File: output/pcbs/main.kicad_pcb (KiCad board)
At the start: 2 copper layers, 121 x 101.5 mm, 62 parts

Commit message: fix PCB + add quirk to readme
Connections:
- _20 pad : GND -> P2
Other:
- net class Default removed

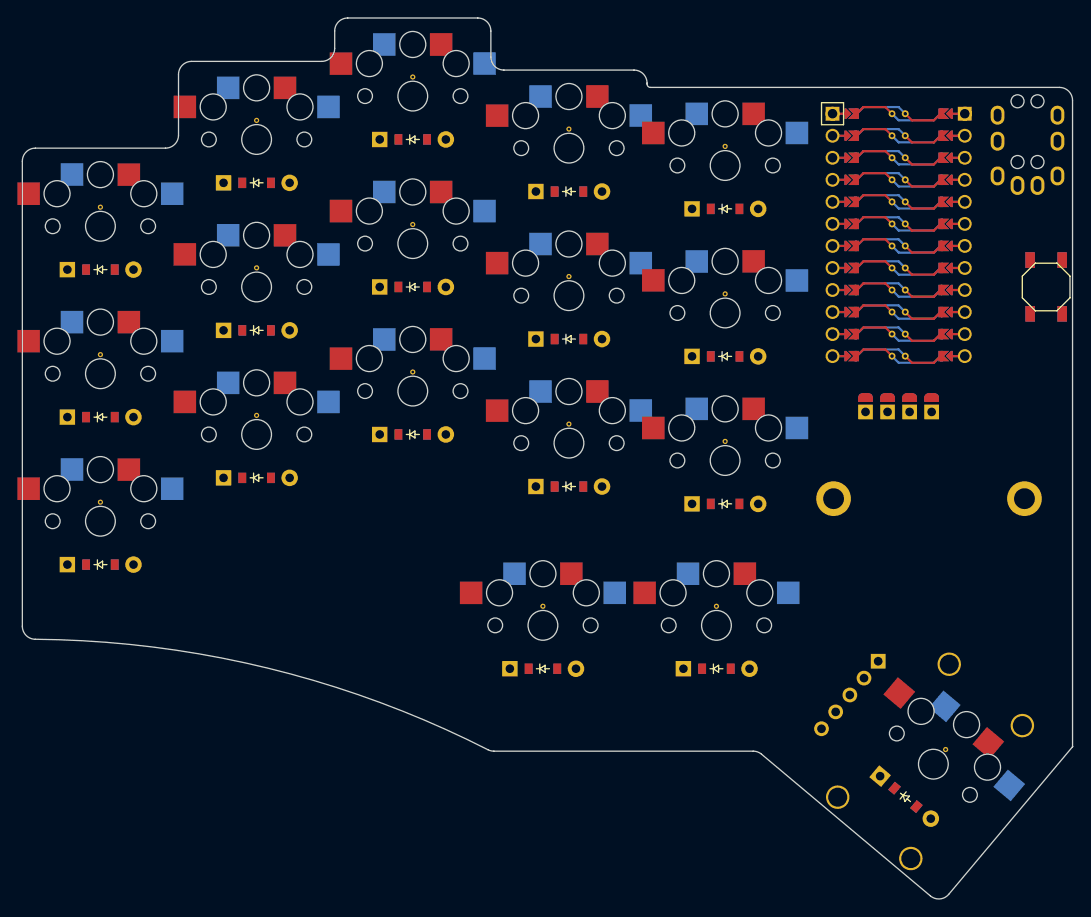
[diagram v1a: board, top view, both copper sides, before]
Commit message: temporary fix to turn trackball around
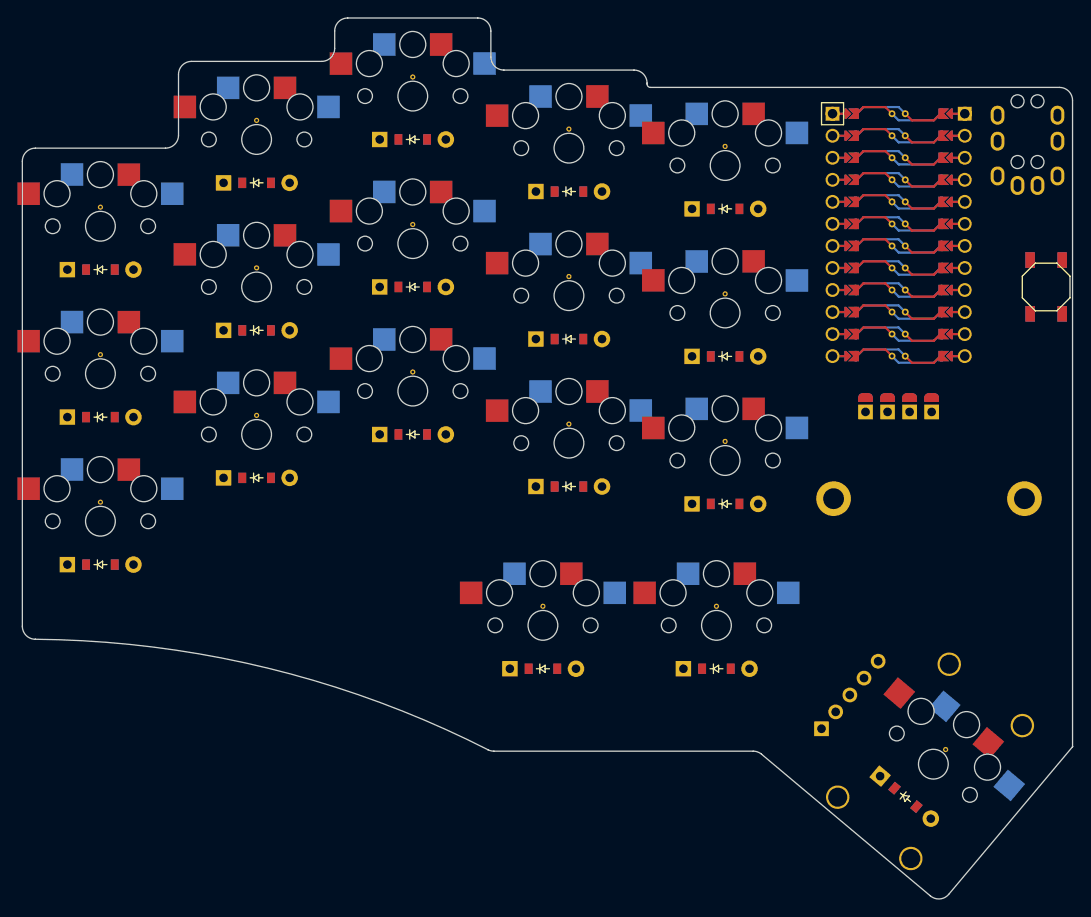
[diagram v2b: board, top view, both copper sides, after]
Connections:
- _20 pad : P2 -> VCC
- _21 pad 3: VCC, -> VCC
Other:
- net class Default added: clearance 0.2, trace_width 0.25, via_dia 0.8, via_drill 0.4

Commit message: whoops the vias were too close
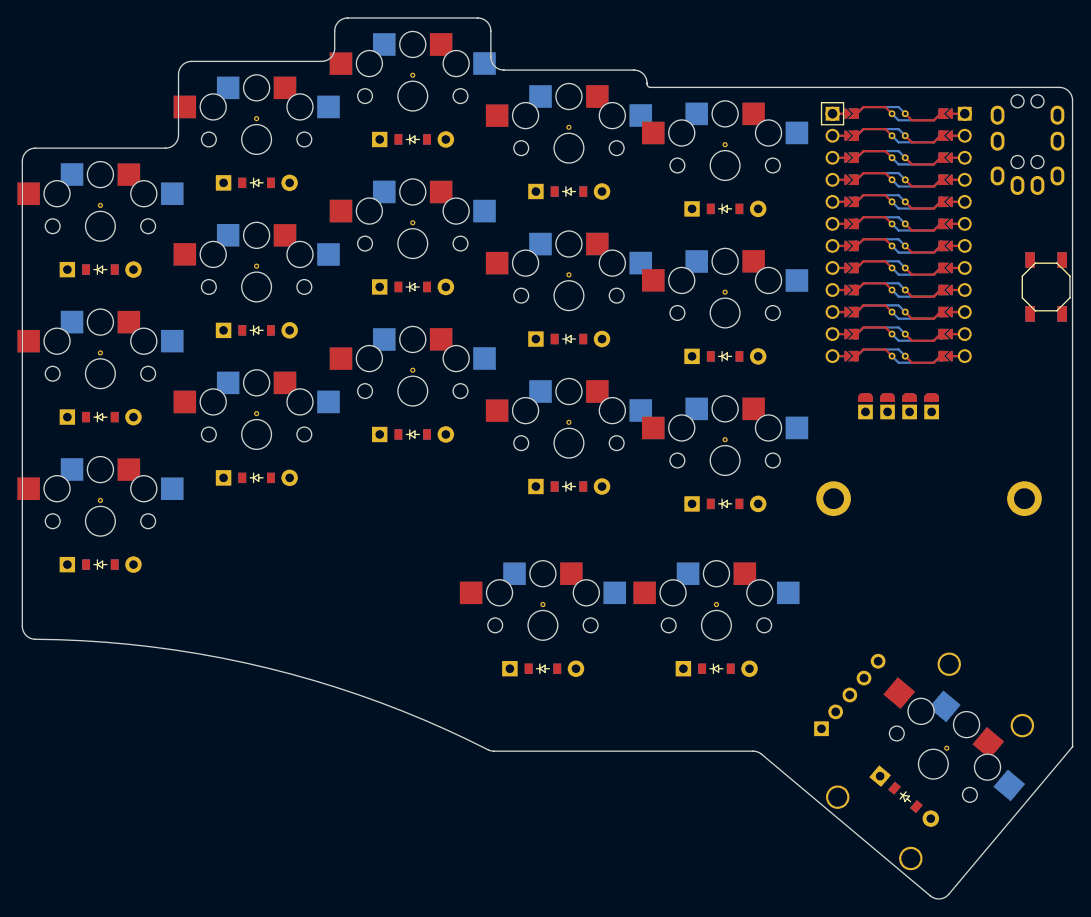
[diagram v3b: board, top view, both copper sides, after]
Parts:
- removed the REF** at (0.00, -2.20)
- removed the REF** at (54.0, -11.2)
- removed the REF** at (54.0, -28.2)
- removed the REF** at (54.0, -45.2)
- removed the REF** at (72.0, -9.20)
- removed the REF** at (72.0, -26.2)
- removed the REF** at (72.0, -43.2)
- removed the REF** at (51.0, 9.80)
- removed the REF** at (71.0, 9.80)
- removed the REF** at (97.4, 26.3)
- removed the REF** at (0.00, -19.2)
- removed the REF** at (0.00, -36.2)
- removed the REF** at (18.0, -12.2)
- removed the REF** at (18.0, -29.2)
- removed the REF** at (18.0, -46.2)
- removed the REF** at (36.0, -17.2)
- removed the REF** at (36.0, -34.2)
- removed the REF** at (36.0, -51.2)
- added REF**: VIA-0.6mm, VIA-0.6mm, F.Cu at (18.0, -46.4)
- added REF**: VIA-0.6mm, VIA-0.6mm, F.Cu at (36.0, -17.4)
- added REF**: VIA-0.6mm, VIA-0.6mm, F.Cu at (71.0, 9.60)
- added REF**: VIA-0.6mm, VIA-0.6mm, F.Cu at (97.5, 26.2)
- added REF**: VIA-0.6mm, VIA-0.6mm, F.Cu at (36.0, -51.4)
- added REF**: VIA-0.6mm, VIA-0.6mm, F.Cu at (72.0, -9.40)
- added REF**: VIA-0.6mm, VIA-0.6mm, F.Cu at (0.00, -19.4)
- added REF**: VIA-0.6mm, VIA-0.6mm, F.Cu at (18.0, -12.4)
- added REF**: VIA-0.6mm, VIA-0.6mm, F.Cu at (51.0, 9.60)
- added REF**: VIA-0.6mm, VIA-0.6mm, F.Cu at (54.0, -11.4)
- added REF**: VIA-0.6mm, VIA-0.6mm, F.Cu at (18.0, -29.4)
- added REF**: VIA-0.6mm, VIA-0.6mm, F.Cu at (54.0, -28.4)
- added REF**: VIA-0.6mm, VIA-0.6mm, F.Cu at (0.00, -36.4)
- added REF**: VIA-0.6mm, VIA-0.6mm, F.Cu at (54.0, -45.4)
- added REF**: VIA-0.6mm, VIA-0.6mm, F.Cu at (0.00, -2.40)
- added REF**: VIA-0.6mm, VIA-0.6mm, F.Cu at (72.0, -43.4)
- added REF**: VIA-0.6mm, VIA-0.6mm, F.Cu at (72.0, -26.4)
- added REF**: VIA-0.6mm, VIA-0.6mm, F.Cu at (36.0, -34.4)
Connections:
- _20 pad : VCC -> P2
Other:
- net class Default removed

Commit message: 2 layer edition featuring gerber files
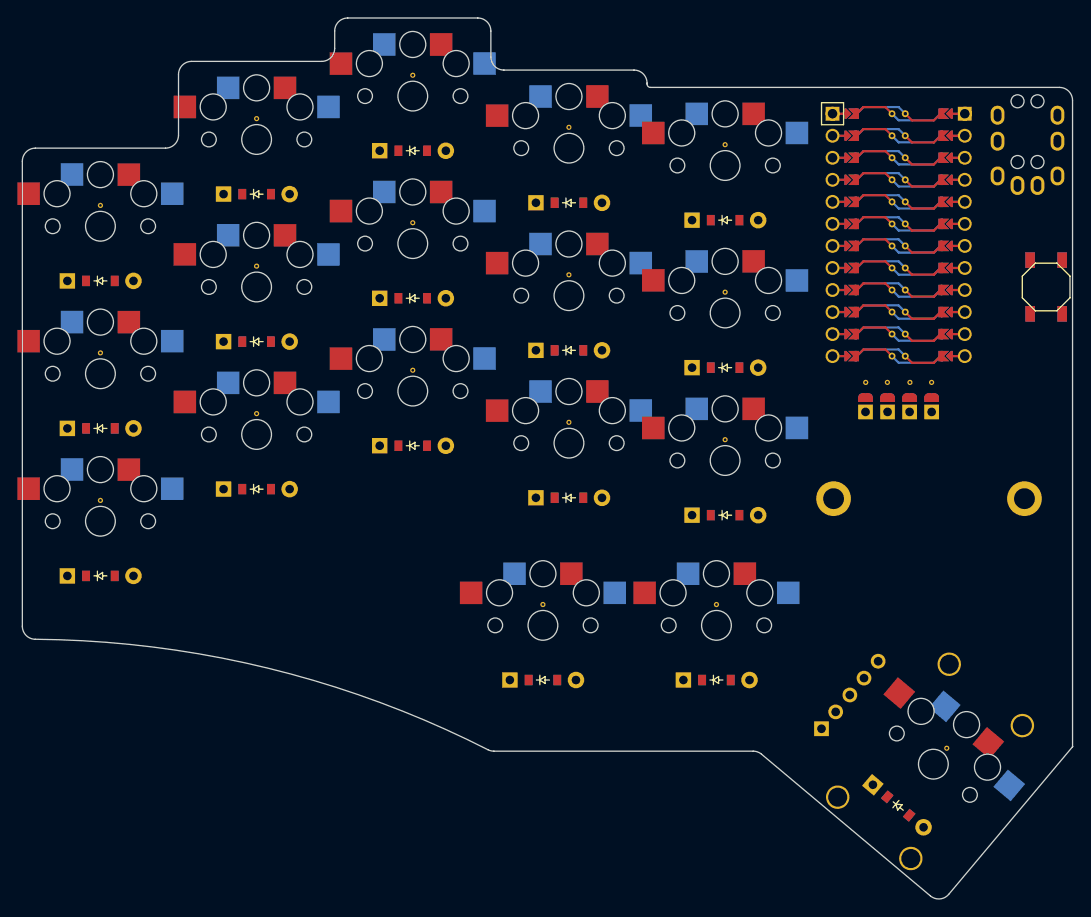
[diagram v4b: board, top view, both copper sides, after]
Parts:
- removed _19: , ProMicro
- removed _20: , pimoroni_trackball
- removed _21: OLED-double-sided, OLED-128x32-double-sided
- added REF**: VIA-0.6mm, VIA-0.6mm, F.Cu at (88.2, -16.0)
- added REF**: VIA-0.6mm, VIA-0.6mm, F.Cu at (90.7, -16.0)
- added REF**: VIA-0.6mm, VIA-0.6mm, F.Cu at (93.3, -16.0)
- added REF**: VIA-0.6mm, VIA-0.6mm, F.Cu at (95.8, -16.0)
- added _23: , ProMicro, F.Cu at (92.0, -33.0)
- added _24: , pimoroni_trackball, F.Cu at (93.7, 26.1)
- added _25: OLED-double-sided, OLED-128x32-double-sided, F.Cu at (86.0, -11.0)
- moved D18 1.30 mm to (92.0, 32.8)
- moved D11 1.30 mm to (54.0, -19.7)
- moved D14 1.30 mm to (72.0, -17.7)
- moved D16 1.30 mm to (51.0, 18.3)
- moved D17 1.30 mm to (71.0, 18.3)
- moved D2 1.30 mm to (0.00, -10.7)
- moved D3 1.30 mm to (0.00, -27.7)
- moved D5 1.30 mm to (18.0, -20.7)
- moved D7 1.30 mm to (36.0, -8.70)
- moved D8 1.30 mm to (36.0, -25.7)
- moved D13 1.30 mm to (72.0, -0.70)
- moved D1 1.30 mm to (0.00, 6.30)
- moved D10 1.30 mm to (54.0, -2.70)
- moved D4 1.30 mm to (18.0, -3.70)
- moved D12 1.30 mm to (54.0, -36.7)
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- renumbered Mount1 to Mount2
